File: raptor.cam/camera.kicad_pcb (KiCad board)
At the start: 2 copper layers, 25 x 28.2 mm, 7 parts

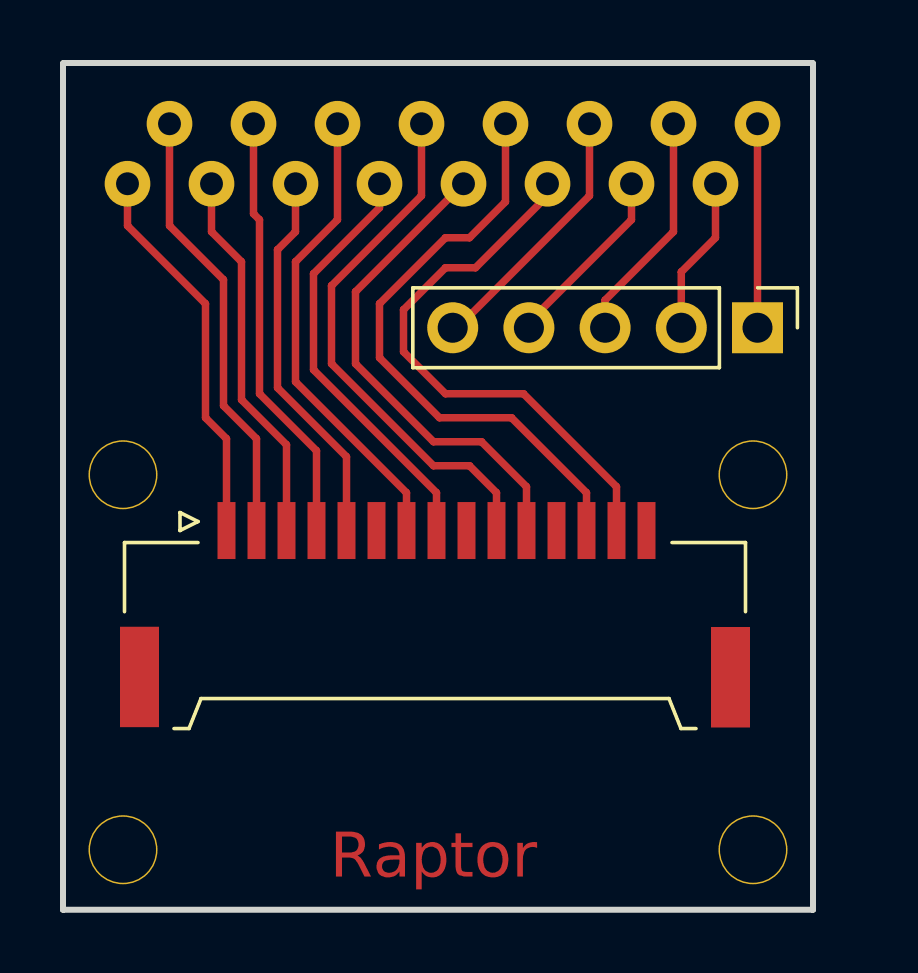
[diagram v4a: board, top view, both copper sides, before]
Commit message: Korekta wymiaru płytki
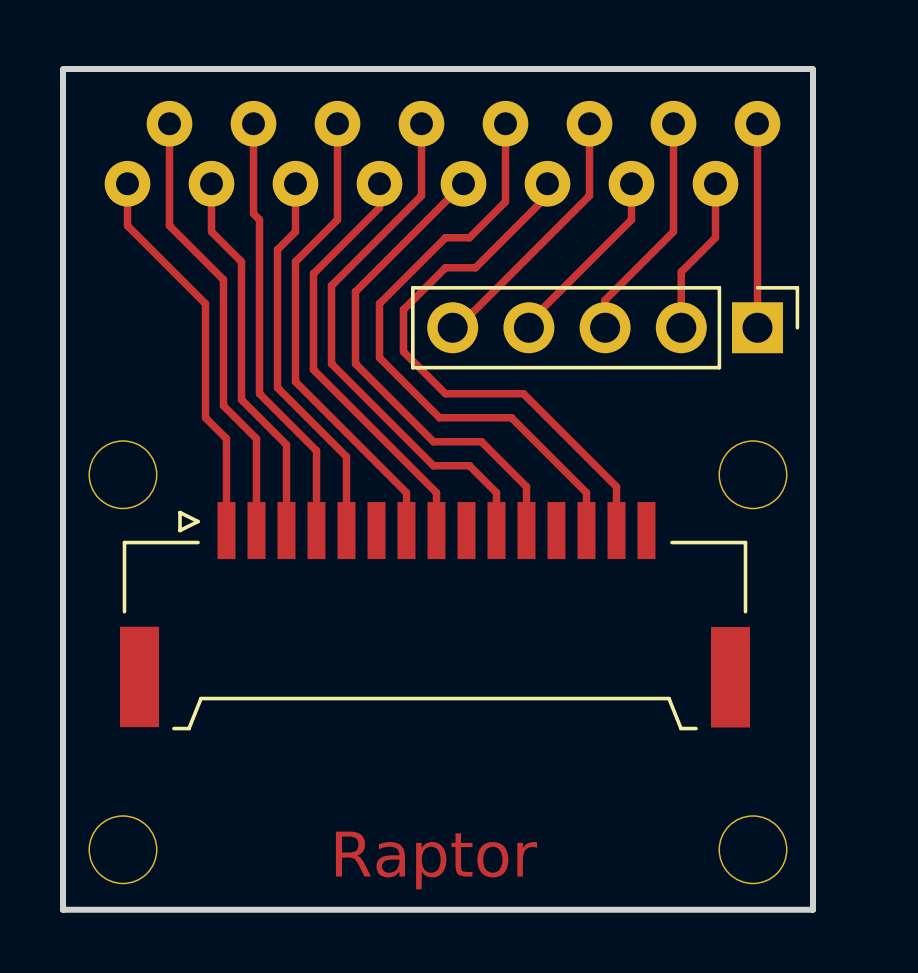
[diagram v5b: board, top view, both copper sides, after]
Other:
- board size 25 x 28.2 mm -> 25 x 28 mm
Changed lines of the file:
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@@
     (area 135.419999 95.674999 163.8 126.885)
     (thickness 1.6)
-    (drawings 6)
+    (drawings 8)
     (tracks 83)
     (zones 0)
@@
       (net 19 "Net-(P2-Pad2)"))
   )
-  (gr_line (start 160.52 124) (end 160.52 95.8) (angle 90) (layer Edge.Cuts) (width 0.2))
+  (dimension 25 (width 0.3) (layer B.Fab)
+    (gr_text "25,000 mm" (at 147.97 129.95) (layer B.Fab)
+      (effects (font (size 1.5 1.5) (thickness 0.3)))
+    )
+    (feature1 (pts (xy 160.47 124) (xy 160.47 131.3)))
+    (feature2 (pts (xy 135.47 124) (xy 135.47 131.3)))
+    (crossbar (pts (xy 135.47 128.6) (xy 160.47 128.6)))
+    (arrow1a (pts (xy 160.47 128.6) (xy 159.343496 129.186421)))
+    (arrow1b (pts (xy 160.47 128.6) (xy 159.343496 128.013579)))
+    (arrow2a (pts (xy 135.47 128.6) (xy 136.596504 129.186421)))
+    (arrow2b (pts (xy 135.47 128.6) (xy 136.596504 128.013579)))
+  )
+  (dimension 28 (width 0.3) (layer B.Fab)
+    (gr_text "28,000 mm" (at 166.22 110 90) (layer B.Fab)
+      (effects (font (size 1.5 1.5) (thickness 0.3)))
+    )
+    (feature1 (pts (xy 160.47 96) (xy 167.57 96)))
+    (feature2 (pts (xy 160.47 124) (xy 167.57 124)))
+    (crossbar (pts (xy 164.87 124) (xy 164.87 96)))
+    (arrow1a (pts (xy 164.87 96) (xy 165.456421 97.126504)))
+    (arrow1b (pts (xy 164.87 96) (xy 164.283579 97.126504)))
+    (arrow2a (pts (xy 164.87 124) (xy 165.456421 122.873496)))
+    (arrow2b (pts (xy 164.87 124) (xy 164.283579 122.873496)))
+  )
+  (gr_line (start 160.52 124) (end 160.52 96) (angle 90) (layer Edge.Cuts) (width 0.2))
   (gr_text Raptor (at 147.87 122.2) (layer F.Cu)
     (effects (font (size 1.5 1.5) (thickness 0.3)))
   )
-  (gr_line (start 160.52 95.775) (end 135.52 95.775) (angle 90) (layer Edge.Cuts) (width 0.2))
+  (gr_line (start 160.52 95.975) (end 135.52 95.975) (angle 90) (layer Edge.Cuts) (width 0.2))
   (gr_circle (center 158.47 122) (end 158.47 123) (layer F.Fab) (width 0.2))
-  (gr_line (start 135.52 124) (end 135.52 95.8) (angle 90) (layer Edge.Cuts) (width 0.2))
+  (gr_line (start 135.52 124) (end 135.52 96) (angle 90) (layer Edge.Cuts) (width 0.2))
   (gr_line (start 160.52 124) (end 135.52 124) (angle 90) (layer Edge.Cuts) (width 0.2))
   (segment (start 140.97 111.36) (end 140.97 108.3) (width 0.25) (layer F.Cu) (net 1))
@@
   (segment (start 140.27 107.6) (end 140.27 103.8) (width 0.25) (layer F.Cu) (net 1))
   (segment (start 140.97 108.3) (end 140.27 107.6) (width 0.25) (layer F.Cu) (net 1))
-  (segment (start 141.97 111.36) (end 141.97 108.3) (width 0.25) (layer F.Cu) (net 2) (status 400000))
-  (segment (start 139.07 101.2) (end 139.07 97.8) (width 0.25) (layer F.Cu) (net 2) (status 800000))
+  (segment (start 141.97 111.36) (end 141.97 108.3) (width 0.25) (layer F.Cu) (net 2))
+  (segment (start 139.07 101.2) (end 139.07 97.8) (width 0.25) (layer F.Cu) (net 2))
   (segment (start 140.87 103) (end 139.07 101.2) (width 0.25) (layer F.Cu) (net 2))
   (segment (start 140.87 107.2) (end 140.87 103) (width 0.25) (layer F.Cu) (net 2))
@@
   (segment (start 142.67 106.6) (end 142.67 102) (width 0.25) (layer F.Cu) (net 5))
   (segment (start 144.97 108.9) (end 142.67 106.6) (width 0.25) (layer F.Cu) (net 5))
-  (segment (start 146.97 111.36) (end 146.97 110.1) (width 0.25) (layer F.Cu) (net 7) (status 400000))
-  (segment (start 144.67 101) (end 144.67 97.8) (width 0.25) (layer F.Cu) (net 7) (status 800000))
+  (segment (start 146.97 111.36) (end 146.97 110.1) (width 0.25) (layer F.Cu) (net 7))
+  (segment (start 144.67 101) (end 144.67 97.8) (width 0.25) (layer F.Cu) (net 7))
   (segment (start 143.27 102.4) (end 144.67 101) (width 0.25) (layer F.Cu) (net 7))
   (segment (start 143.27 106.4) (end 143.27 102.4) (width 0.25) (layer F.Cu) (net 7))
@@
   (segment (start 149.07 109.2) (end 147.87 109.2) (width 0.25) (layer F.Cu) (net 10))
   (segment (start 149.97 110.1) (end 149.07 109.2) (width 0.25) (layer F.Cu) (net 10))
-  (segment (start 150.97 111.36) (end 150.97 109.9) (width 0.25) (layer F.Cu) (net 11) (status 400000))
-  (segment (start 145.27 103.4) (end 148.87 99.8) (width 0.25) (layer F.Cu) (net 11) (status 800000))
+  (segment (start 150.97 111.36) (end 150.97 109.9) (width 0.25) (layer F.Cu) (net 11))
+  (segment (start 145.27 103.4) (end 148.87 99.8) (width 0.25) (layer F.Cu) (net 11))
   (segment (start 145.27 105.8) (end 145.27 103.4) (width 0.25) (layer F.Cu) (net 11))
   (segment (start 147.87 108.4) (end 145.27 105.8) (width 0.25) (layer F.Cu) (net 11))
@@
   (segment (start 150.47 107.6) (end 148.07 107.6) (width 0.25) (layer F.Cu) (net 13))
   (segment (start 152.97 110.1) (end 150.47 107.6) (width 0.25) (layer F.Cu) (net 13))
-  (segment (start 153.97 111.36) (end 153.97 109.9) (width 0.25) (layer F.Cu) (net 14) (status 400000))
-  (segment (start 149.27 102.6) (end 151.67 100.2) (width 0.25) (layer F.Cu) (net 14) (status 800000))
+  (segment (start 153.97 111.36) (end 153.97 109.9) (width 0.25) (layer F.Cu) (net 14))
+  (segment (start 149.27 102.6) (end 151.67 100.2) (width 0.25) (layer F.Cu) (net 14))
   (segment (start 148.27 102.6) (end 149.27 102.6) (width 0.25) (layer F.Cu) (net 14))
   (segment (start 146.87 104) (end 148.27 102.6) (width 0.25) (layer F.Cu) (net 14))
@@
   (segment (start 150.87 106.8) (end 148.27 106.8) (width 0.25) (layer F.Cu) (net 14))
   (segment (start 153.97 109.9) (end 150.87 106.8) (width 0.25) (layer F.Cu) (net 14))
-  (segment (start 151.67 100.2) (end 151.67 99.8) (width 0.25) (layer F.Cu) (net 14) (status C00000))
+  (segment (start 151.67 100.2) (end 151.67 99.8) (width 0.25) (layer F.Cu) (net 14))
   (segment (start 153.59 104.6) (end 153.59 103.68) (width 0.25) (layer F.Cu) (net 16))
   (segment (start 155.87 101.4) (end 155.87 97.8) (width 0.25) (layer F.Cu) (net 16))
   (segment (start 153.59 103.68) (end 155.87 101.4) (width 0.25) (layer F.Cu) (net 16))
   (segment (start 152.99 104.6) (end 153.47 104.6) (width 0.25) (layer F.Cu) (net 16))
-  (segment (start 151.05 104.6) (end 151.05 104.42) (width 0.25) (layer F.Cu) (net 17) (status C00000))
-  (segment (start 151.05 104.42) (end 154.47 101) (width 0.25) (layer F.Cu) (net 17) (status 400000))
-  (segment (start 154.47 101) (end 154.47 99.8) (width 0.25) (layer F.Cu) (net 17) (status 800000))
-  (segment (start 151.05 104.6) (end 151.27 104.6) (width 0.25) (layer F.Cu) (net 17) (status C00000))
+  (segment (start 151.05 104.6) (end 151.05 104.42) (width 0.25) (layer F.Cu) (net 17))
+  (segment (start 151.05 104.42) (end 154.47 101) (width 0.25) (layer F.Cu) (net 17))
+  (segment (start 154.47 101) (end 154.47 99.8) (width 0.25) (layer F.Cu) (net 17))
+  (segment (start 151.05 104.6) (end 151.27 104.6) (width 0.25) (layer F.Cu) (net 17))
   (segment (start 150.45 104.6) (end 150.47 104.6) (width 0.25) (layer F.Cu) (net 17))
-  (segment (start 148.51 104.6) (end 148.67 104.6) (width 0.25) (layer F.Cu) (net 18) (status C00000))
-  (segment (start 148.67 104.6) (end 153.07 100.2) (width 0.25) (layer F.Cu) (net 18) (status 400000))
-  (segment (start 153.07 100.2) (end 153.07 97.8) (width 0.25) (layer F.Cu) (net 18) (status 800000))
+  (segment (start 148.51 104.6) (end 148.67 104.6) (width 0.25) (layer F.Cu) (net 18))
+  (segment (start 148.67 104.6) (end 153.07 100.2) (width 0.25) (layer F.Cu) (net 18))
+  (segment (start 153.07 100.2) (end 153.07 97.8) (width 0.25) (layer F.Cu) (net 18))
   (segment (start 147.91 104.6) (end 147.91 104.56) (width 0.25) (layer F.Cu) (net 18))
   (segment (start 156.13 104.6) (end 156.13 102.74) (width 0.25) (layer F.Cu) (net 19))

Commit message: Gotowy negatyw pcb adaptera.
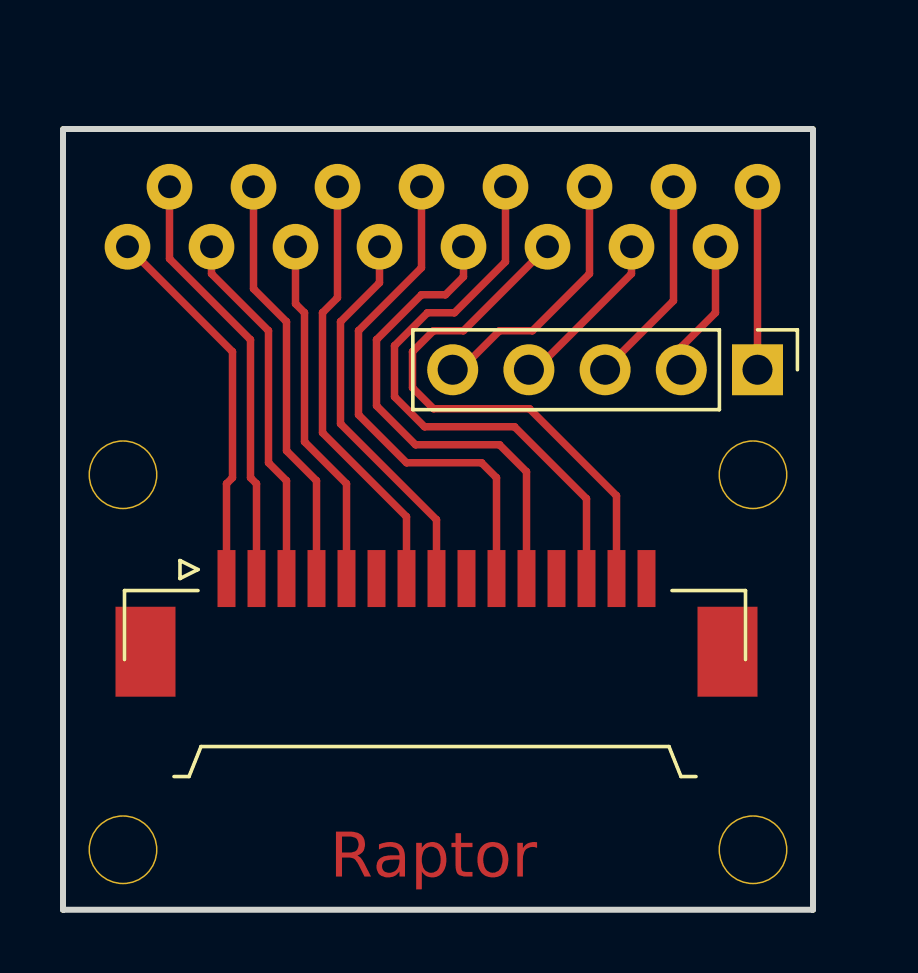
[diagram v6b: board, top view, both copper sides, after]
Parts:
- moved ? 2.10 mm to (148.3, 102.9)
- moved ? 1.60 mm to (147.9, 115.4)
- moved ? 1.40 mm to (158.7, 106.0)
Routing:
- net Net-(P1-Pad7): track 15.7 -> 14.4 mm
- net Net-(P2-Pad3): track 8.22 -> 7.04 mm
- net Net-(P1-Pad5): track 12.8 -> 11.8 mm
- net Net-(P2-Pad4): track 6.46 -> 5.65 mm
- net Net-(P1-Pad8): track 14.2 -> 13.4 mm
- net Net-(P2-Pad2): track 5.27 -> 4.57 mm
- net Net-(P2-Pad1): track 6.80 -> 6.10 mm
- net Net-(P1-Pad13): track 20.0 -> 19.5 mm
- net Net-(P1-Pad3): track 12.6 -> 12.1 mm
- net Net-(P1-Pad2): track 14.8 -> 14.3 mm
- net Net-(P1-Pad4): track 14.4 -> 13.9 mm
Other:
- board size 25 x 28 mm -> 25 x 26 mm
